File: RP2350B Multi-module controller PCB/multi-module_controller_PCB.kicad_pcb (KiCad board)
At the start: 4 copper layers, 59.8 x 84.4 mm, 79 parts, among them J1 Conn_02x06_Odd_Even, J4 SM03B-SRSS-TB, J5 USB_C_Receptacle_USB2.0_14P, J6 USB_C_Receptacle_USB2.0_14P, J7 Module_Bay, J8 USB_A, J9 ADC_Breakout, SW1 SW_Push, SW10 BTN_MDL, SW2 SW_Push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

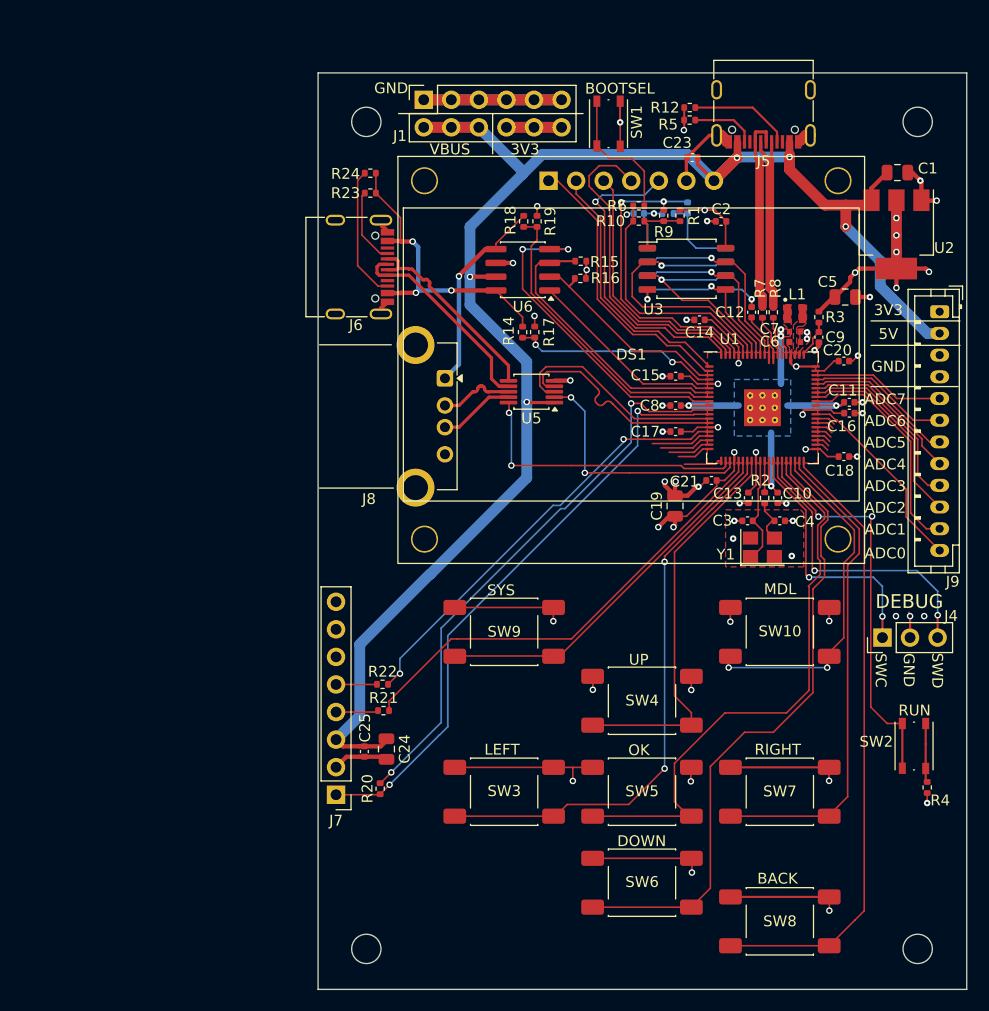
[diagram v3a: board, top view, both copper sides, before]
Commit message: adjust GPIO breakout, add LED, silkscreen labels, etc
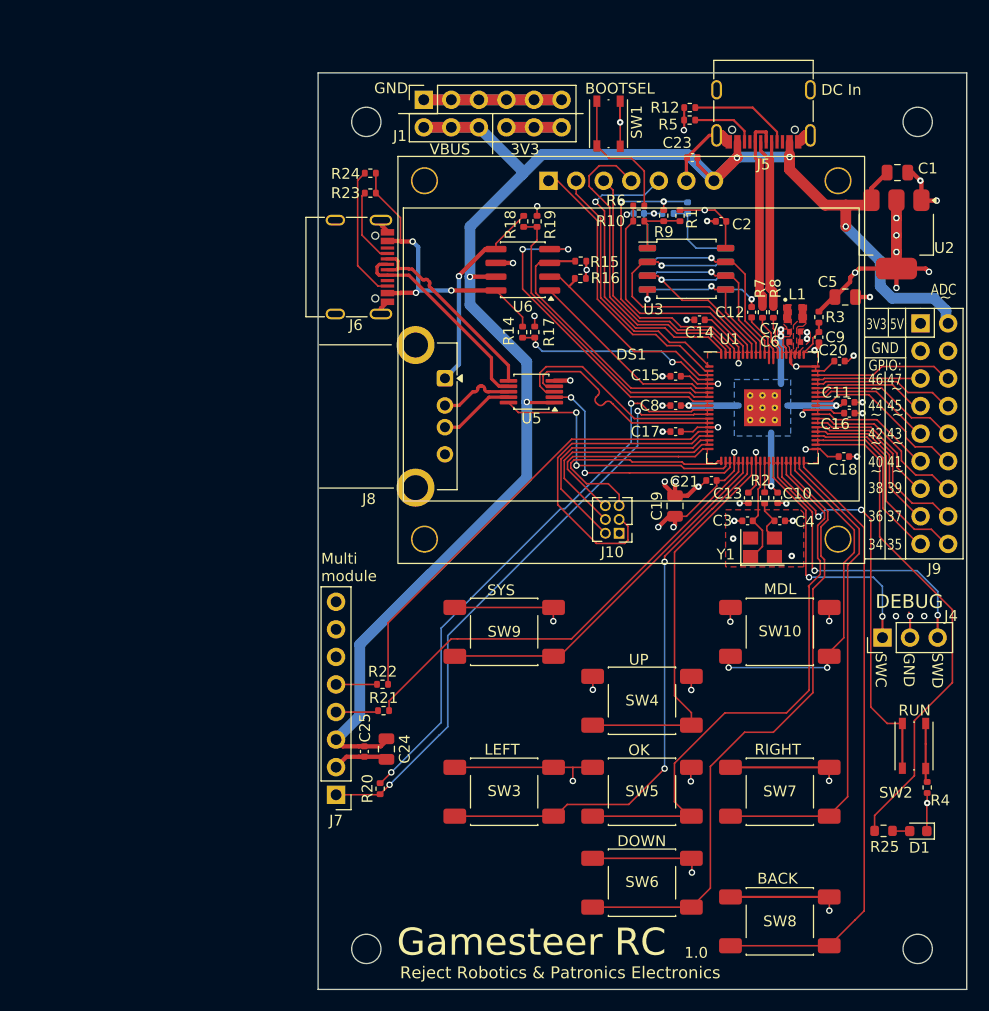
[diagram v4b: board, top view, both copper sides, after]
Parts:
- added D1: LED, LED_SMD:LED_0603_1608Metric, F.Cu at (114.4, 139.0)
- added J10: Internal unused GPIO Breakout, Connector_PinHeader_1.27mm:PinHeader_2x03_P1.27mm_Vertical, F.Cu at (86.8, 111.6)
- added R25: 220, Resistor_SMD:R_0603_1608Metric, F.Cu at (111.2, 139.0)
- J9: footprint Connector_JST:JST_PH_B12B-PH-K_1x12_P2.00mm_Vertical -> Connector_PinHeader_2.54mm:PinHeader_2x09_P2.54mm_Vertical
- moved J9 2.06 mm to (114.6, 92.2), turned to 0 degrees
- moved C20 0.40 mm to (107.1, 95.7)
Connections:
- J9 pad 10: /GPIO42_ADC2 -> /GPIO43_ADC3
- J9 pad 11: /GPIO41_ADC1 -> /GPIO40_ADC0
- J9 pad 12: /GPIO40_ADC0 -> /GPIO41_ADC1
- J9 pad 5: /GPIO47_ADC7 -> /GPIO46_ADC6
- J9 pad 6: /GPIO46_ADC6 -> /GPIO47_ADC7
- J9 pad 7: /GPIO45_ADC5 -> /GPIO44_ADC4
- J9 pad 8: /GPIO44_ADC4 -> /GPIO45_ADC5
- J9 pad 9: /GPIO43_ADC3 -> /GPIO42_ADC2
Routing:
- net /GPIO33: track 1.31 -> 46.4 mm
- net /GPIO17: track 5.54 -> 29.5 mm
- net /GPIO18: track 4.79 -> 22.9 mm
- net /GPIO21: track 3.53 -> 21.2 mm
- net /GPIO35: track 1.51 -> 18.5 mm
- net /GPIO19: track 4.00 -> 21.0 mm
- net /GPIO20: track 3.14 -> 19.1 mm
- net /GPIO37: track 1.71 -> 17.0 mm
- net /GPIO34: track 1.41 -> 16.2 mm
- net /GPIO39: track 1.91 -> 15.2 mm
- net /GPIO36: track 1.61 -> 14.5 mm
- net /GPIO38: track 1.81 -> 12.7 mm
- net /GPIO42_ADC2: track 18.3 -> 11.3 mm
- net /GPIO40_ADC0: track 18.1 -> 11.3 mm
- net /GPIO41_ADC1: track 20.7 -> 15.1 mm
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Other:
- board text added: "1.0"
- board text added: "34 35"
- board text added: "35 34"
- board text added: "36 37"
- board text added: "37 36"
- board text added: "38 39"
- board text added: "39 38"
- board text added: "40 41"
- board text added: "41 40"
- board text added: "42 43"
- board text added: "43 42"
- board text added: "44 45"
- board text added: "45 44"
- board text added: "46 47"
- board text added: "47 46"
- board text added: "ADC"
- board text added: "DC In"
- board text added: "From Joshua Adriano and Patrick Leiser"
- board text added: "GPIO:"
- board text added: "Gamesteer RC"
- board text added: "J10"
- board text added: "J9"
- board text added: "Multi module"
- board text added: "Reject Robotics & Patronics Electronics"
- board text added: "~"
- board text removed: "ADC0"
- board text removed: "ADC1"
- board text removed: "ADC2"
- board text removed: "ADC3"
- board text removed: "ADC4"
- board text removed: "ADC5"
- board text removed: "ADC6"
- board text removed: "ADC7"

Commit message: add date to silkscreen
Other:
- board text added: "V1.0 2025-2026"
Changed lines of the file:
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@@
+		)
+	)
+	(gr_text "V1.0      2025-2026"
+		(at 89.1 152.7 0)
+		(layer "B.SilkS")
+		(effects
+			(font
+				(size 1 1)
+				(thickness 0.15)
+			)
+			(justify left bottom mirror)
 		)
 	)

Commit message: Implement pin-remapping and adjustments for new PCB, add support for both USB A and C ports (configured at compile-time by active_usb_port for now). Buttons, i2c display, USB A, USB C, all functional. Multi-module adjustments WIP
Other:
- board text added: "REV 2 TODO: Shift multi-module port down slightly to avoid overlap with USB A port"
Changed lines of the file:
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@@
+		)
+	)
+	(gr_text "REV 2 TODO:\nShift multi-module port down slightly\nto avoid overlap with USB A port"
+		(at 57 125.5 0)
+		(layer "Dwgs.User")
+		(effects
+			(font
+				(size 2 2)
+				(thickness 0.25)
+			)
+			(justify right bottom)
 		)
 	)

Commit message: start on revisions for REV2 board design
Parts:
- added R26: 22, Resistor_SMD:R_0402_1005Metric, F.Cu at (66.8, 135.6)
- R20: value 680 -> 22
- R21, R22: value 330 -> 22
- R25: value 220 -> 470
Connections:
- J7 pad 1: /GPIO13 -> Net-(J7-Pin_1)
- R20 pad 1: /GPIO13 -> Net-(J7-Pin_1)
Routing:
- net Net-(J7-Pin_1): track 0.00 -> 5.27 mm
- net /GPIO13: track 55.8 -> 50.9 mm

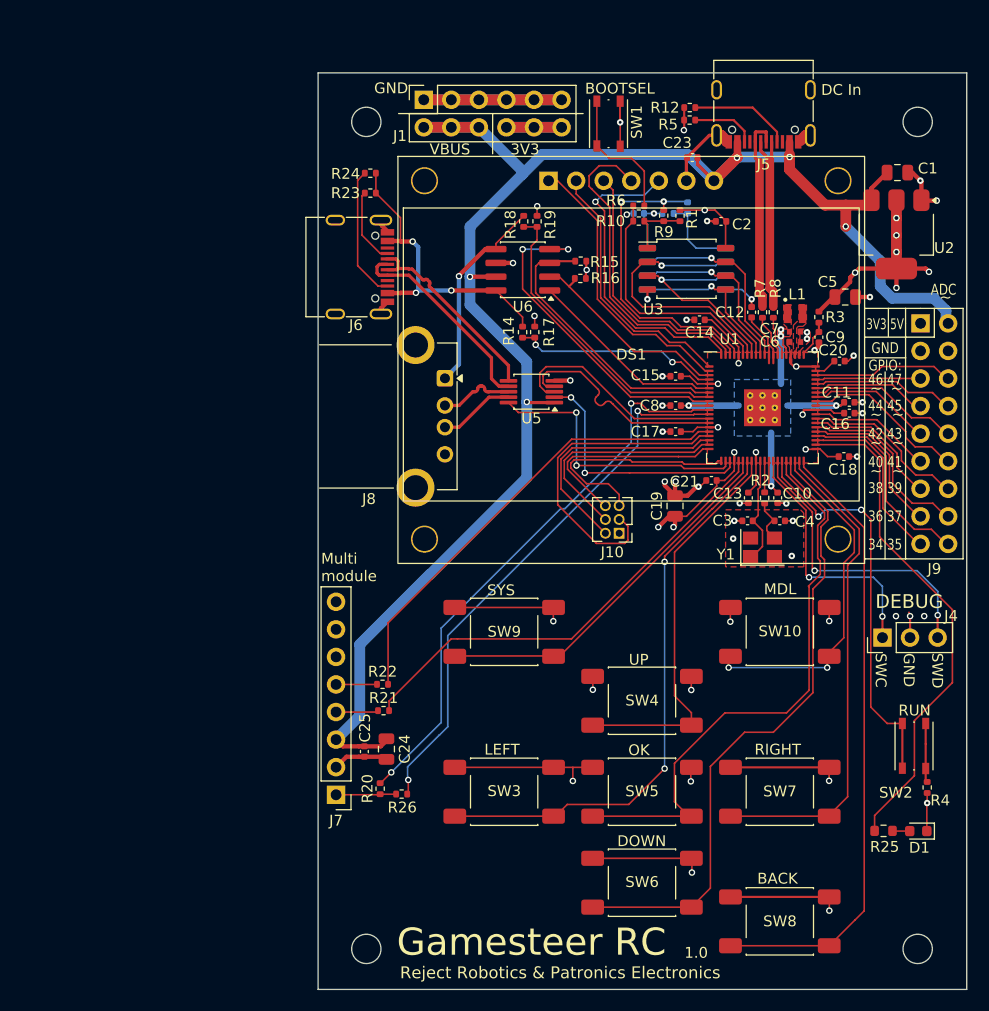
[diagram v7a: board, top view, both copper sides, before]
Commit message: Update PCB with improved bulk capacitors for VBus, increased mounting hole diameter for display, and offset multi-module connector further away from USB A port
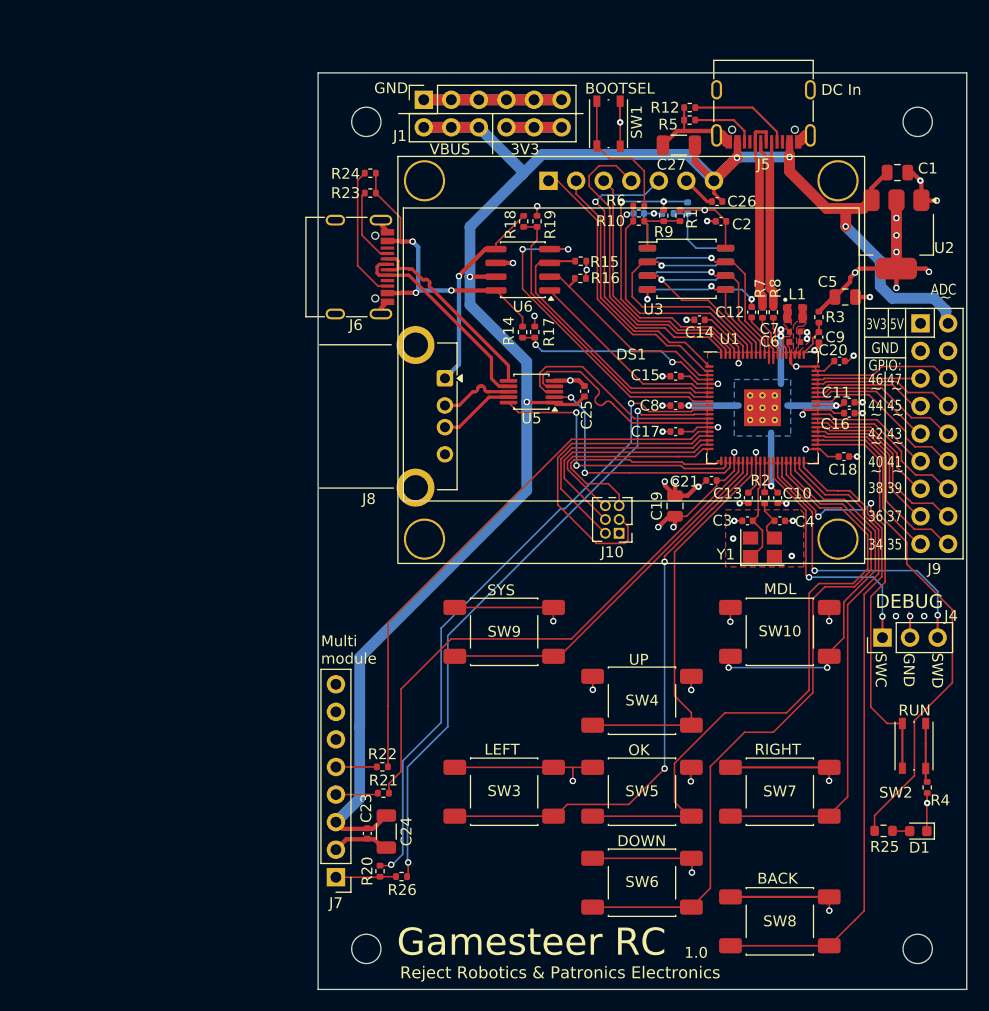
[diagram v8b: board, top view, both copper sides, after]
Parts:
- added C26: 100n, Capacitor_SMD:C_0402_1005Metric, F.Cu at (95.8, 81.0)
- added C27: 47u, Capacitor_SMD:C_1206_3216Metric, F.Cu at (92.3, 75.8)
- C24: footprint Capacitor_SMD:C_0805_2012Metric -> Capacitor_SMD:C_1206_3216Metric
- moved C23 69.1 mm to (63.6, 139.2), turned to -90 degrees
- moved C25 38.9 mm to (83.6, 98.5), turned to 90 degrees
- moved R21 7.60 mm to (65.1, 135.5)
- moved R22 7.60 mm to (65.0, 133.1)
- moved C24 7.60 mm to (65.3, 139.1)
- moved J7 7.60 mm to (60.7, 143.3)
- moved R20 7.60 mm to (64.8, 142.7)
- moved R26 7.60 mm to (66.7, 143.2)
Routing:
- net VBUS: track 156.2 -> 171.9 mm
- net /GPIO12: track 52.5 -> 60.6 mm
- net /GPIO24: track 42.8 -> 50.4 mm
- net /GPIO13: track 50.9 -> 58.5 mm
- net /GPIO16: track 42.6 -> 50.2 mm
- net /GPIO28: track 53.3 -> 59.4 mm
- net /GPIO29: track 58.7 -> 64.5 mm
- net GND: track 150.6 -> 156.0 mm, vias 47 -> 46
- net /GPIO31: track 45.3 -> 48.0 mm
- net /GPIO30: track 32.6 -> 35.4 mm
- net /GPIO32: track 57.4 -> 60.0 mm
- net /RUN: track 36.9 -> 39.4 mm
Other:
- board text removed: "REV 2 TODO: Shift multi-module port down slightly to avoid overlap with USB A port"
